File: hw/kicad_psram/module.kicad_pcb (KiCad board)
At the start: 8 copper layers, 110 x 70 mm, 20 parts

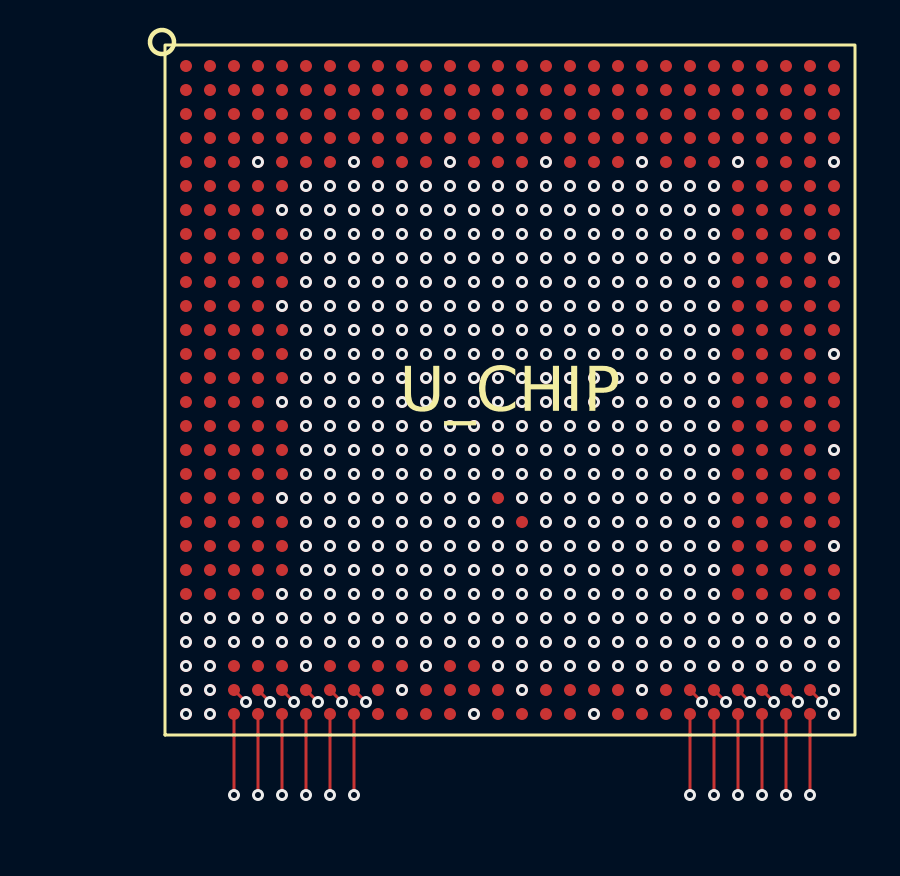
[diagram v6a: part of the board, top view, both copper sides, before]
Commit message: Move the PSRAM clock balls to the north edge beside the memory
A small interface may now name its own package edge in
package_selection.edges; psram_clk: N puts the sixteen clocks in the row
just inside the north memory rows, sixteen of its eighteen positions
between the east and west strips, so each clock escapes with its memory
and runs 15 to 55 mm to its device instead of round the package.  The
report lists them and counts them among the balls that need a build-up
escape.  The clock study keeps the south placement as its second case
and sweeps the point-to-point trace over the north lengths.

Co-Authored-By: Claude Fable 5.1 <noreply@anthropic.com>
Claude-Session: https://claude.ai/code/session_01VmmvkZe8Ctg3RAykNGsQBn
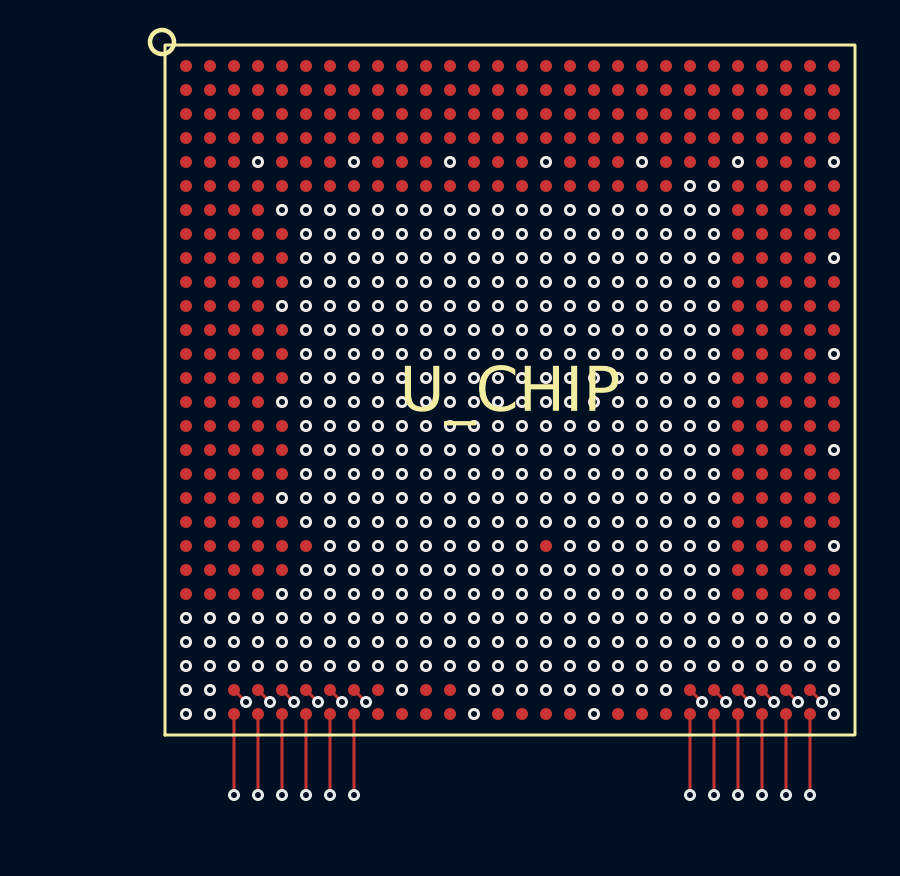
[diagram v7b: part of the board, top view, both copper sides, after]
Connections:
- U_CHIP pad AA16: VDD_CORE -> VDD_PLL_0V9
- U_CHIP pad AA6: VDD_CORE -> VDD_PLL_0V9
- U_CHIP pad AF10: PSRAM_CLK13 -> GND
- U_CHIP pad AF11: GND -> VDD_CORE
- U_CHIP pad AF12: PSRAM_CLK14 -> GND
- U_CHIP pad AF13: PSRAM_CLK15 -> VDD_CORE
- U_CHIP pad AF3: PSRAM_CLK7 -> VDD_CORE
- U_CHIP pad AF4: PSRAM_CLK8 -> GND
- U_CHIP pad AF5: PSRAM_CLK9 -> VDD_CORE
- U_CHIP pad AF7: PSRAM_CLK10 -> VDD_CORE
- U_CHIP pad AF8: PSRAM_CLK11 -> GND
- U_CHIP pad AF9: PSRAM_CLK12 -> VDD_CORE
- U_CHIP pad AG13: PSRAM_CLK0 -> GND
- U_CHIP pad AG14: PSRAM_CLK1 -> VDD_CORE
- U_CHIP pad AG16: PSRAM_CLK2 -> VDD_CORE
- U_CHIP pad AG17: PSRAM_CLK3 -> GND
- U_CHIP pad AG18: PSRAM_CLK4 -> VDD_CORE
- U_CHIP pad AG19: PSRAM_CLK5 -> GND
- U_CHIP pad AG20: GND -> VDD_CORE
- U_CHIP pad AG21: PSRAM_CLK6 -> GND
- U_CHIP pad F10: GND -> PSRAM_CLK4
- U_CHIP pad F11: VDD_IO_1V8 -> PSRAM_CLK5
- U_CHIP pad F12: GND -> PSRAM_CLK6
- U_CHIP pad F13: VDD_CORE -> PSRAM_CLK7
- U_CHIP pad F14: GND -> PSRAM_CLK8
- U_CHIP pad F15: VDD_CORE -> PSRAM_CLK9
- U_CHIP pad F16: GND -> PSRAM_CLK10
- U_CHIP pad F17: VDD_CORE -> PSRAM_CLK11
- U_CHIP pad F18: GND -> PSRAM_CLK12
- U_CHIP pad F19: VDD_CORE -> PSRAM_CLK13
- U_CHIP pad F20: GND -> PSRAM_CLK14
- U_CHIP pad F21: VDD_IO_1V8 -> PSRAM_CLK15
- U_CHIP pad F6: GND -> PSRAM_CLK0
- U_CHIP pad F7: VDD_CORE -> PSRAM_CLK1
- U_CHIP pad F8: GND -> PSRAM_CLK2
- U_CHIP pad F9: VDD_CORE -> PSRAM_CLK3
- U_CHIP pad W14: VDD_PLL_0V9 -> VDD_IO_1V8
- U_CHIP pad Y15: VDD_PLL_0V9 -> VDD_IO_1V8
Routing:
- net VDD_CORE: vias 181 -> 183
- net GND: vias 282 -> 280
